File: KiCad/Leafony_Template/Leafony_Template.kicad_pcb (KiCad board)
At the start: 4 copper layers, 20 x 20 mm, 1 part, among them CN1 Leafony bus

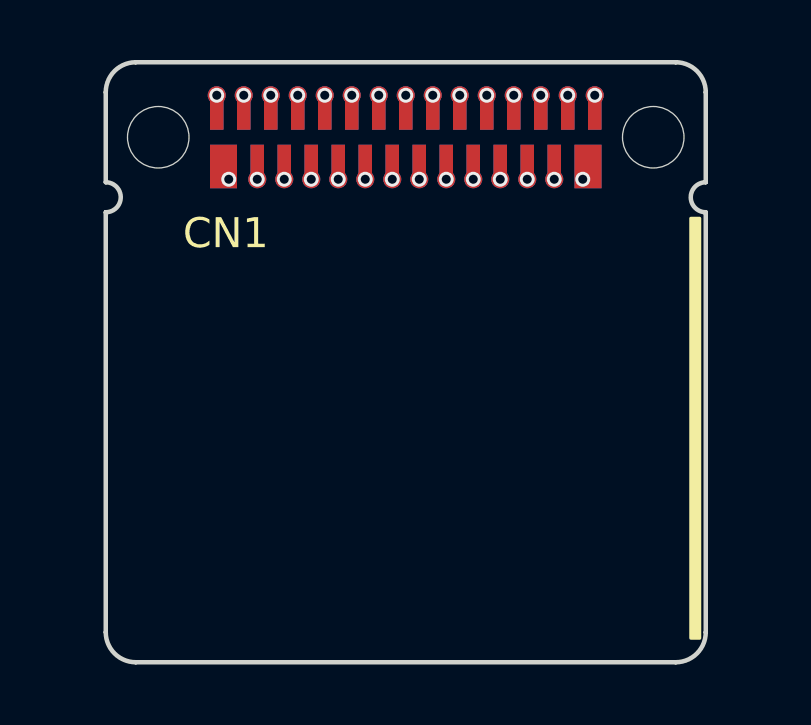
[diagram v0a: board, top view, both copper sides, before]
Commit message: Update KiCad Template
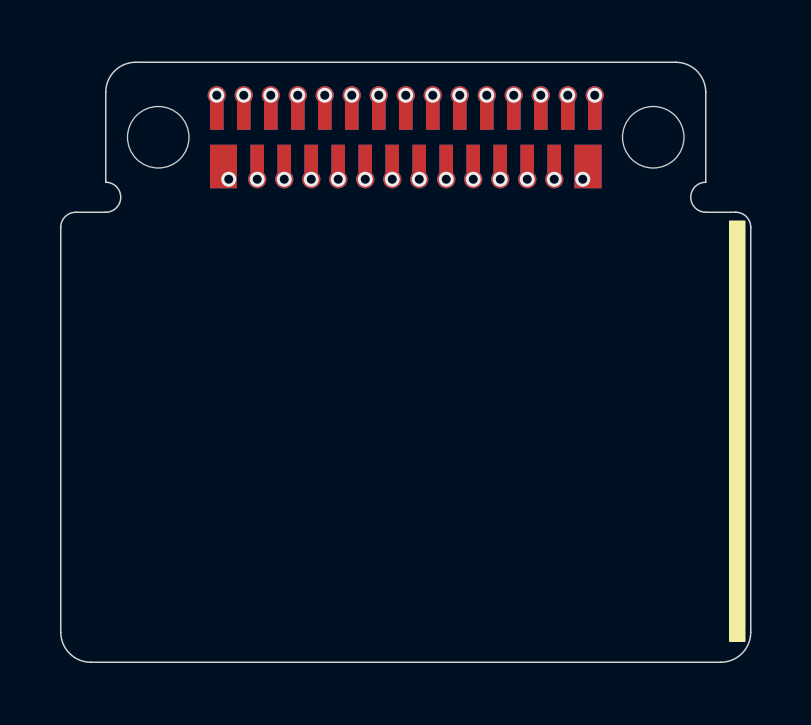
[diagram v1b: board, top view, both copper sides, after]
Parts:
- CN1: value Leafony bus -> Leafony Bus
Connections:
- net +3.3V renamed +3V3
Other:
- board size 20 x 20 mm -> 23 x 20 mm
- rule pad_to_mask_clearance: 0.1 -> 0.05
